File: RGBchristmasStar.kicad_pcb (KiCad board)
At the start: 2 copper layers, 190 x 180.7 mm, 45 parts, among them U1 WeMos_D1_mini

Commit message: created new footprints
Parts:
- D1, D10, D11, D12, D13, D14, D15, D16, D17, D18, D19, D2, D20, D21, D22, D3, D4, D5, D6, D7, D8, D9: footprint LED_SMD:LED_WS2812B_PLCC4_5.0x5.0mm_P3.2mm -> lib_fp:WS2812B-Mini
- U1: footprint Module:WEMOS_D1_mini_light -> lib_fp:WEMOS_D1_mini_light_SMD_header; moved to B.Cu
- moved C1 223.8 mm to (-7.84, 59.4)
- moved D1 192.2 mm to (-7.84, 63.2)
- moved C10 122.7 mm to (88.5, 37.7)
- moved C12 122.7 mm to (97.4, 34.1)
- moved C14 122.7 mm to (88.5, 34.7)
- moved C16 122.7 mm to (88.5, 31.7)
- moved C3 122.7 mm to (97.4, 31.1)
- moved C4 122.7 mm to (88.5, 40.7)
- moved C5 122.7 mm to (101.4, 28.1)
- moved C6 122.7 mm to (84.5, 44.9)
- moved C9 122.7 mm to (101.4, 25.0)
- moved D10 122.7 mm to (82.1, 40.1)
- moved D11 122.7 mm to (73.7, 33.5)
- moved D12 122.7 mm to (82.1, 26.8)
- moved D15 122.7 mm to (82.1, 20.2)
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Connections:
- D22 pad 2: Net-(D22-Pad2) -> (no net)
- U1 pad 1: Net-(U1-Pad1) -> (no net)
- U1 pad 12: Net-(U1-Pad12) -> (no net)
- U1 pad 13: Net-(U1-Pad13) -> (no net)
- U1 pad 14: Net-(U1-Pad14) -> (no net)
- U1 pad 15: Net-(U1-Pad15) -> (no net)
- U1 pad 16: Net-(U1-Pad16) -> (no net)
- U1 pad 2: Net-(U1-Pad2) -> (no net)
- U1 pad 3: Net-(U1-Pad3) -> (no net)
- U1 pad 4: Net-(U1-Pad4) -> (no net)
- U1 pad 5: Net-(U1-Pad5) -> (no net)
- U1 pad 6: Net-(U1-Pad6) -> (no net)
- U1 pad 7: Net-(U1-Pad7) -> (no net)
- U1 pad 8: Net-(U1-Pad8) -> (no net)
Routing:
- net GND: track 0.00 -> 4.49 mm, vias 0 -> 2
- net +5V: track 0.00 -> 3.28 mm

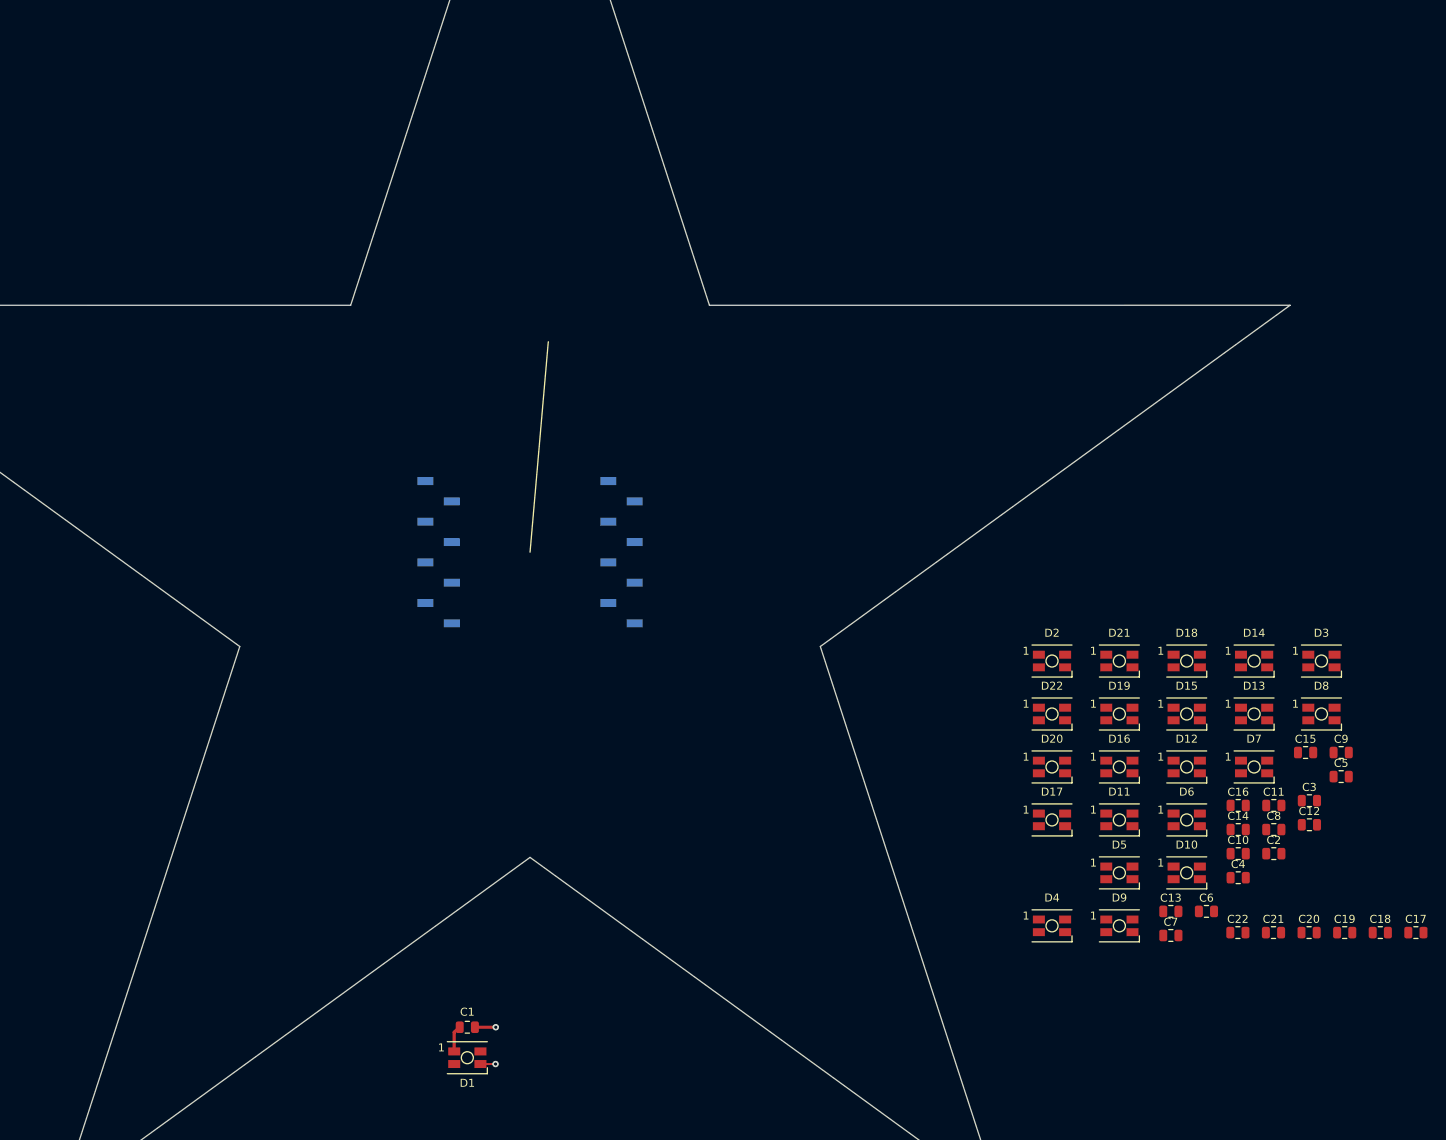
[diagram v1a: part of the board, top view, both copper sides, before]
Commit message: Update RGBchristmasStar.kicad_pcb
Placed LEDs in star with ciruclar array script
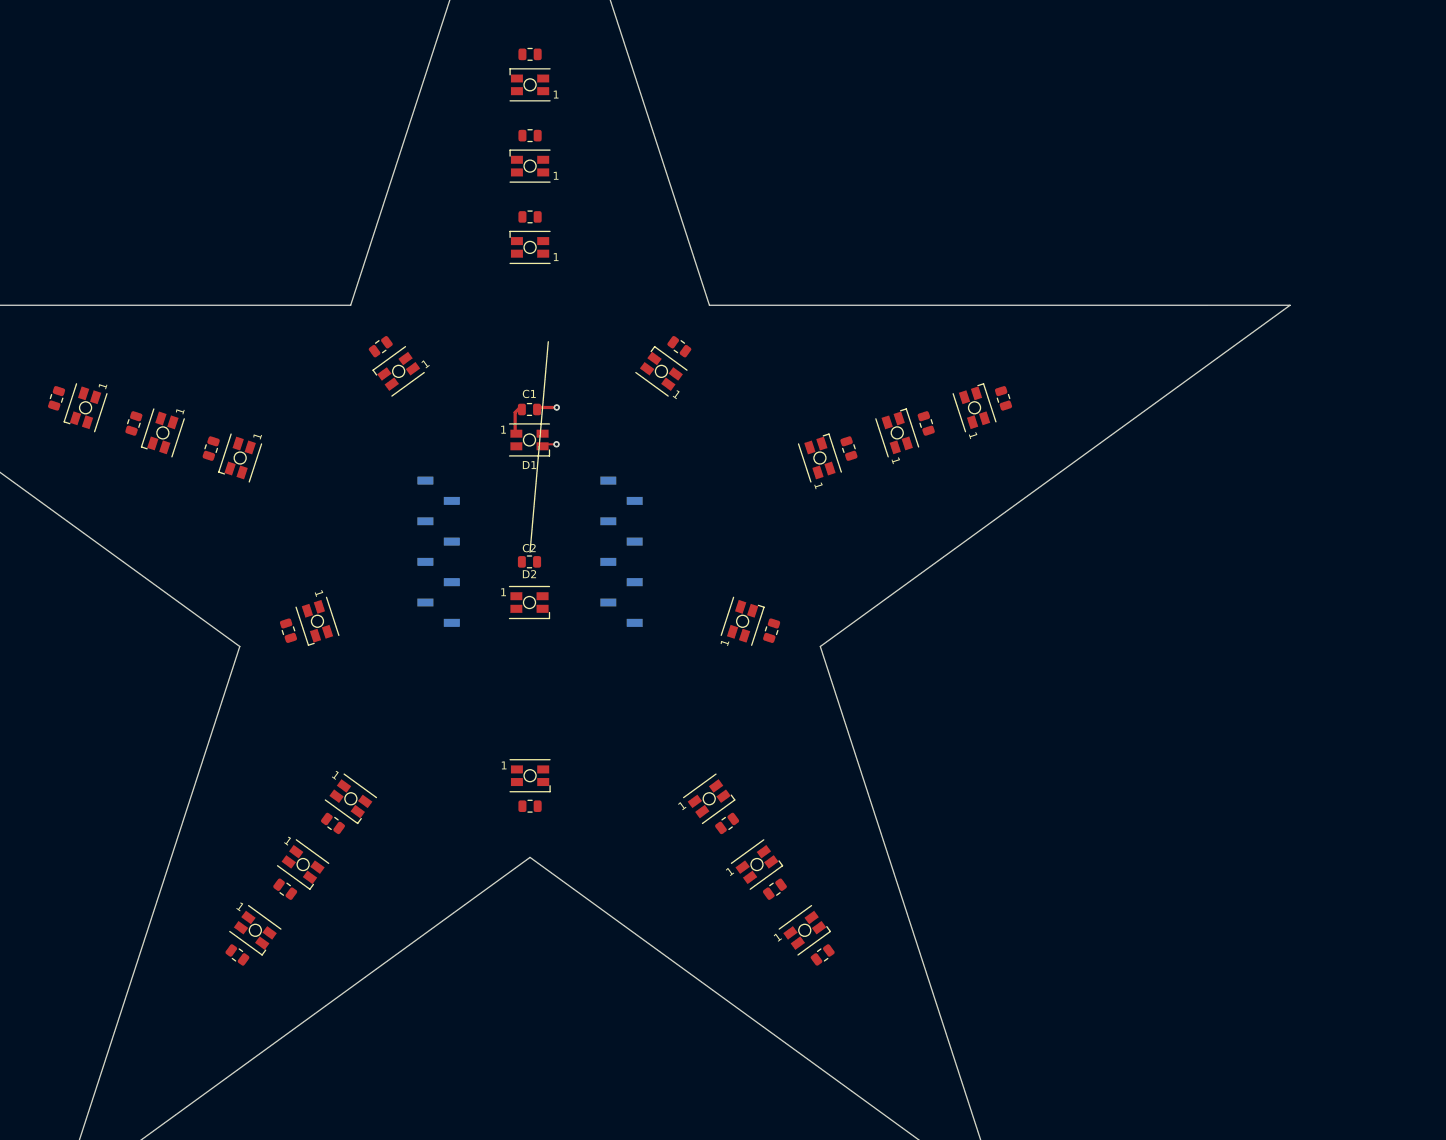
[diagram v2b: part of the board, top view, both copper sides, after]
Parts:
- moved C10 158.3 mm to (-59.2, -19.2), turned to 252 degrees
- moved C9 156.4 mm to (-49.5, -16.1), turned to 252 degrees
- moved D10 149.4 mm to (-55.6, -18.1), turned to 252 degrees
- moved C8 141.1 mm to (-39.9, -13.0), turned to 252 degrees
- moved D8 138.9 mm to (-36.2, -11.8), turned to 252 degrees
- moved D9 134.5 mm to (-45.9, -14.9), turned to 252 degrees
- moved C5 132.7 mm to (-30.6, 42.1), turned to 324 degrees
- moved C14 131.2 mm to (0.00, -62.2), turned to 180 degrees
- moved C13 125.8 mm to (0.00, -52.1), turned to 180 degrees
- moved C11 125.5 mm to (-18.7, -25.7), turned to 216 degrees
- moved C12 123.5 mm to (0.00, -41.9), turned to 180 degrees
- moved C6 121.3 mm to (-36.6, 50.3), turned to 324 degrees
- moved D7 118.5 mm to (-26.6, 8.63), turned to 288 degrees
- moved D6 117.2 mm to (-34.3, 47.3), turned to 324 degrees
- moved C7 116.7 mm to (-30.2, 9.81), turned to 288 degrees
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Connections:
- D22 pad 2: (no net) -> Net-(D22-Pad2)
- U1 pad 1: (no net) -> Net-(U1-Pad1)
- U1 pad 12: (no net) -> Net-(U1-Pad12)
- U1 pad 13: (no net) -> Net-(U1-Pad13)
- U1 pad 14: (no net) -> Net-(U1-Pad14)
- U1 pad 15: (no net) -> Net-(U1-Pad15)
- U1 pad 16: (no net) -> Net-(U1-Pad16)
- U1 pad 2: (no net) -> Net-(U1-Pad2)
- U1 pad 3: (no net) -> Net-(U1-Pad3)
- U1 pad 4: (no net) -> Net-(U1-Pad4)
- U1 pad 5: (no net) -> Net-(U1-Pad5)
- U1 pad 6: (no net) -> Net-(U1-Pad6)
- U1 pad 7: (no net) -> Net-(U1-Pad7)
- U1 pad 8: (no net) -> Net-(U1-Pad8)

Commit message: Changed position of components + added routing + pours + fiducials + made silkscreen visible
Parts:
- added REF**: Fiducial_1mm_Mask2mm, Fiducial:Fiducial_1mm_Mask2mm, F.Cu at (95.5, 134.7)
- added REF**: Fiducial_1mm_Mask2mm, Fiducial:Fiducial_1mm_Mask2mm, F.Cu at (120.5, 134.7)
- added REF**: Fiducial_1mm_Mask2mm, Fiducial:Fiducial_1mm_Mask2mm, F.Cu at (108.0, 88.0)
- moved C11 166.4 mm to (95.3, 95.5)
- moved C8 165.3 mm to (77.8, 103.2)
- moved C9 164.2 mm to (66.9, 99.7)
- moved C12 163.8 mm to (108.0, 81.2)
- moved C10 163.1 mm to (56.1, 96.1)
- moved C13 162.9 mm to (108.0, 69.8)
- moved C1 162.3 mm to (104.1, 106.6), turned to 90 degrees
- moved C14 161.9 mm to (108.0, 58.4)
- moved D1 161.9 mm to (107.9, 106.6), turned to 90 degrees
- moved C7 161.0 mm to (87.5, 119.7)
- moved D11 158.8 mm to (93.1, 92.5)
- moved D8 158.6 mm to (74.2, 102.0)
- moved C15 158.4 mm to (120.7, 95.5)
- moved D12 158.2 mm to (108.0, 77.4)
- moved C2 157.5 mm to (104.1, 119.3), turned to 90 degrees
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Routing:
- net GND: track 4.49 -> 93.5 mm, vias 2 -> 44
- net Net-(D18-Pad2): track 0.00 -> 48.1 mm
- net Net-(D14-Pad2): track 0.00 -> 48.1 mm
- net Net-(D6-Pad2): track 0.00 -> 48.1 mm
- net Net-(D10-Pad2): track 0.00 -> 48.1 mm
- net Net-(D19-Pad2): track 0.00 -> 22.4 mm, vias 0 -> 2
- net Net-(D3-Pad2): track 0.00 -> 22.4 mm, vias 0 -> 2
- net Net-(D7-Pad2): track 0.00 -> 22.4 mm, vias 0 -> 2
- net Net-(D15-Pad2): track 0.00 -> 22.4 mm, vias 0 -> 2
- net Net-(D11-Pad2): track 0.00 -> 22.4 mm, vias 0 -> 2
- net Net-(D2-Pad2): track 0.00 -> 22.2 mm
- net Din: track 0.00 -> 19.6 mm, vias 0 -> 1
- net Net-(D8-Pad2): track 0.00 -> 17.3 mm
- net Net-(D10-Pad4): track 0.00 -> 17.3 mm
- net Net-(D17-Pad2): track 0.00 -> 17.3 mm
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- added copper zone on F.Cu, net +5V
- added copper zone on B.Cu, net GND

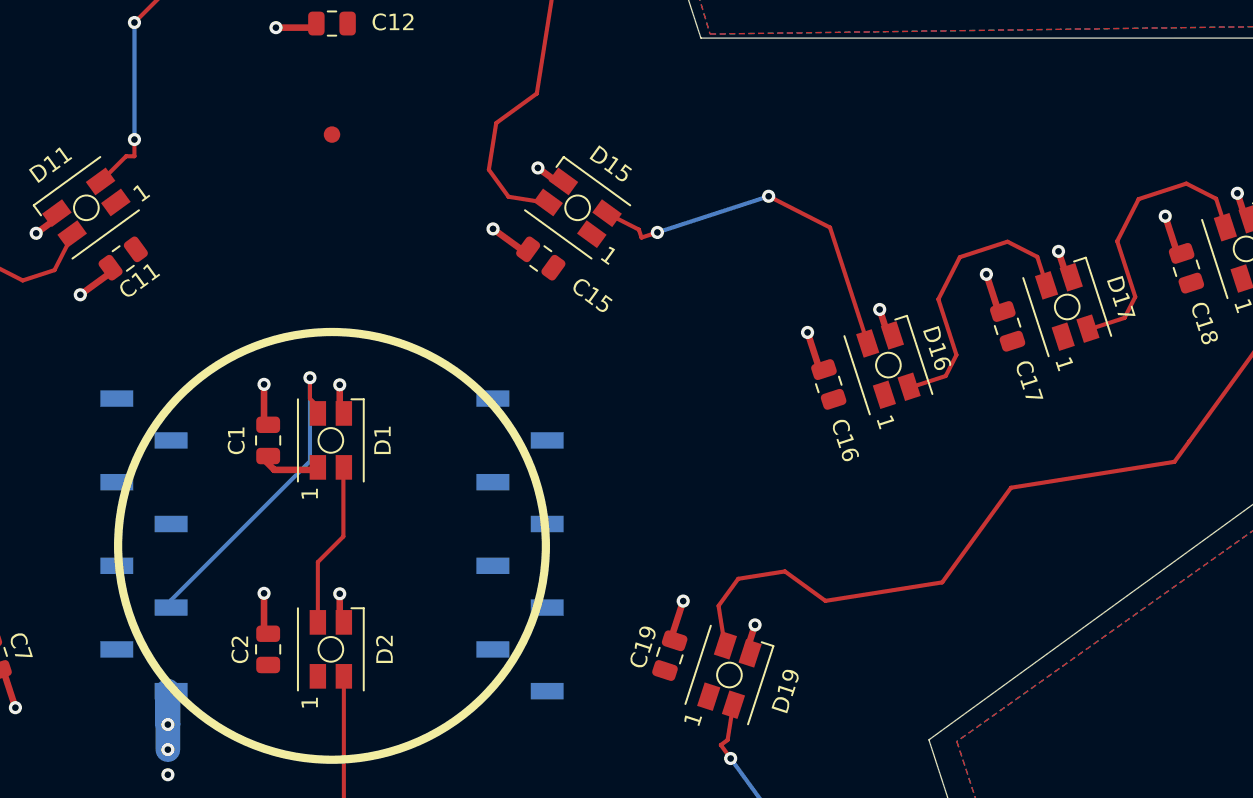
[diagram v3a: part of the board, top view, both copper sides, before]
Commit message: first commit to JLCPCB with SMT
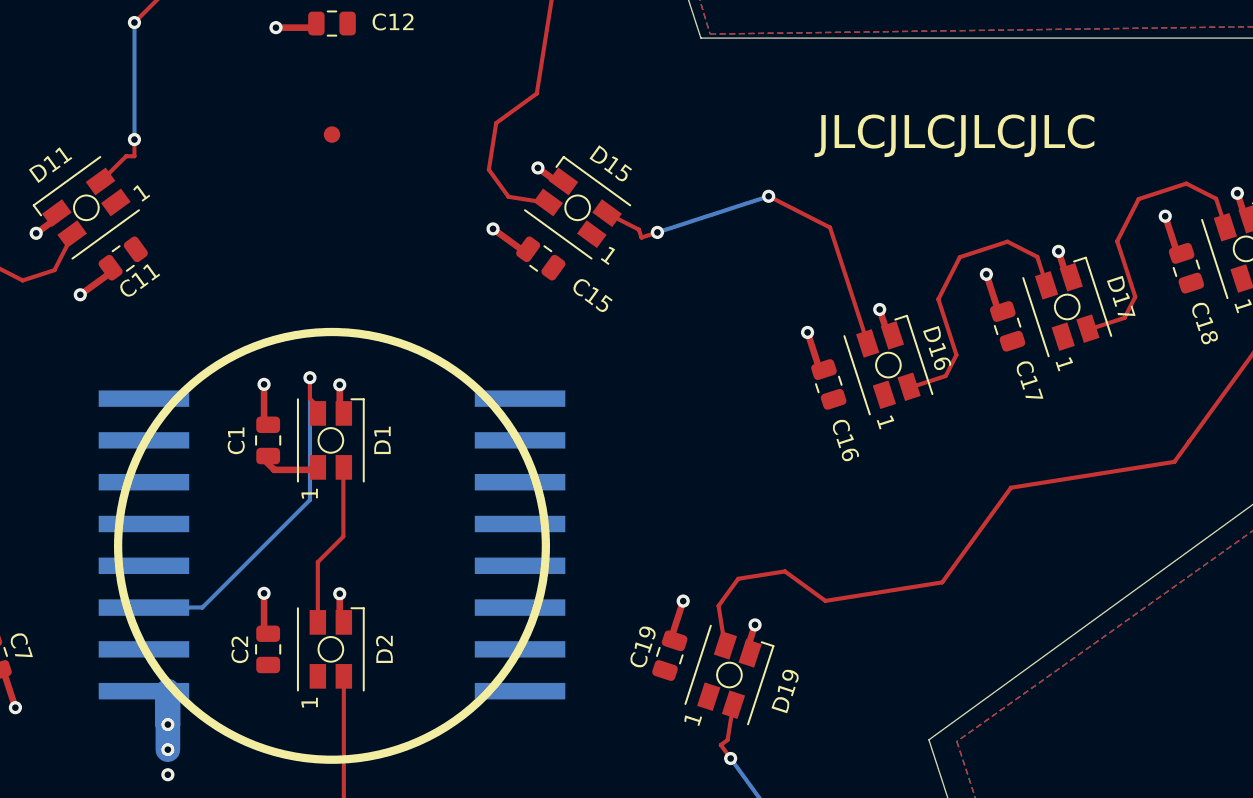
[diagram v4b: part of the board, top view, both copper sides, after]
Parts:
- added REF**: OSHW-Logo2_14.6x12mm_SilkScreen, Symbol:OSHW-Logo2_14.6x12mm_SilkScreen, B.Cu at (108.0, 40.0)
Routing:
- net Din: track 19.6 -> 20.7 mm
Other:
- board text added: "JLCJLCJLCJLC"
- board text added: "https://github.com/vacuumSpark/RGBchristmasStar"
